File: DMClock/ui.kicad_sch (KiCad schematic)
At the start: 142 parts, among them U3 HV5622PG-G, U4 HV5622PG-G, U5 HV5622PG-G

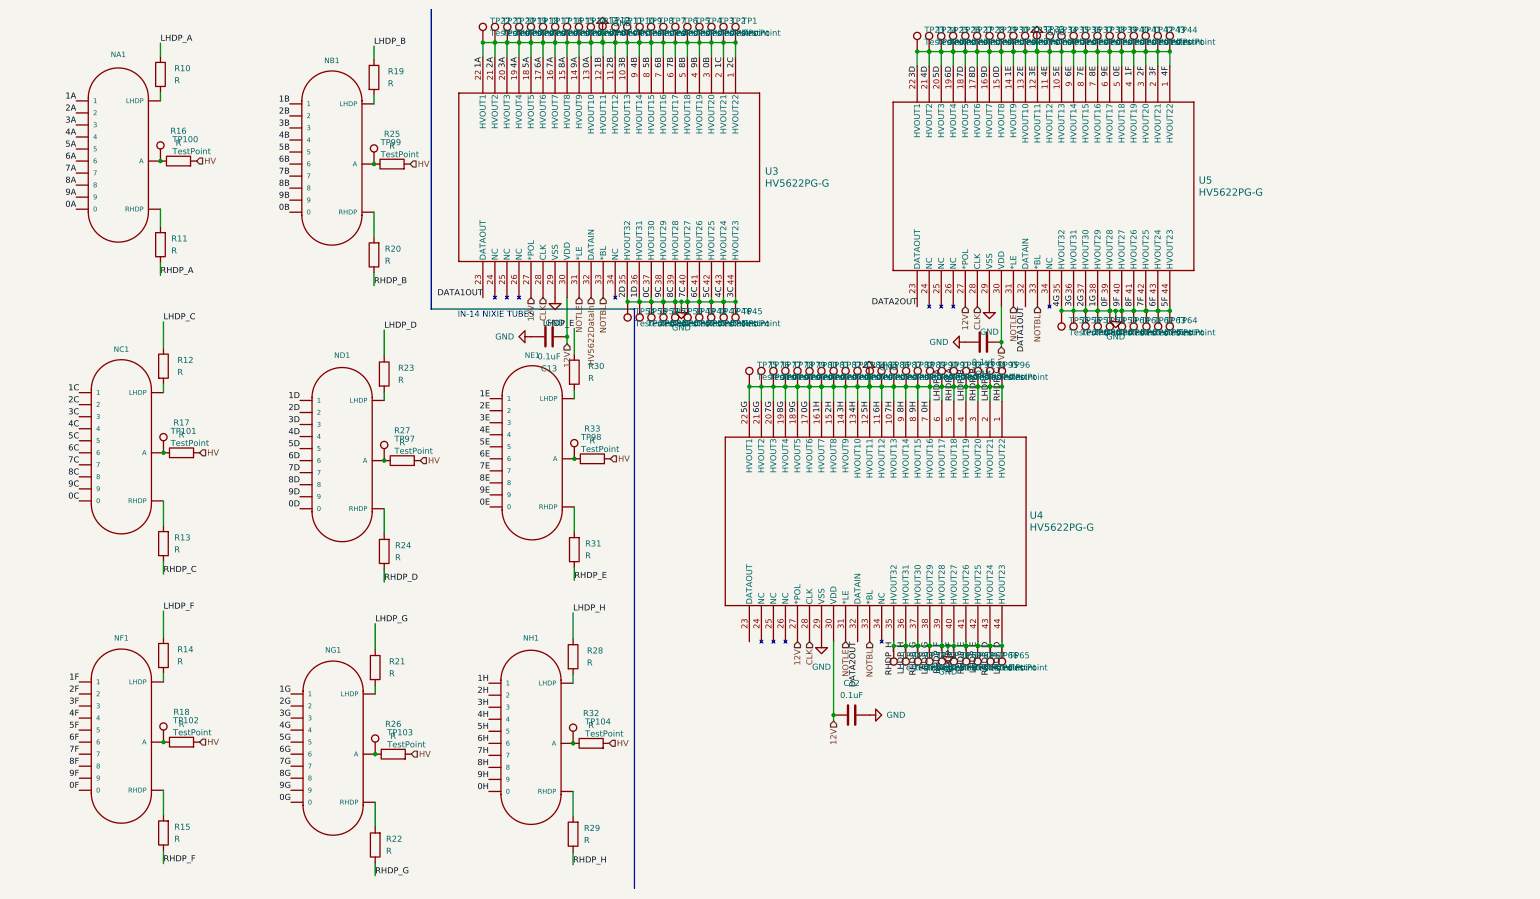
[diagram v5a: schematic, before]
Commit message: added test points, need to fix commas
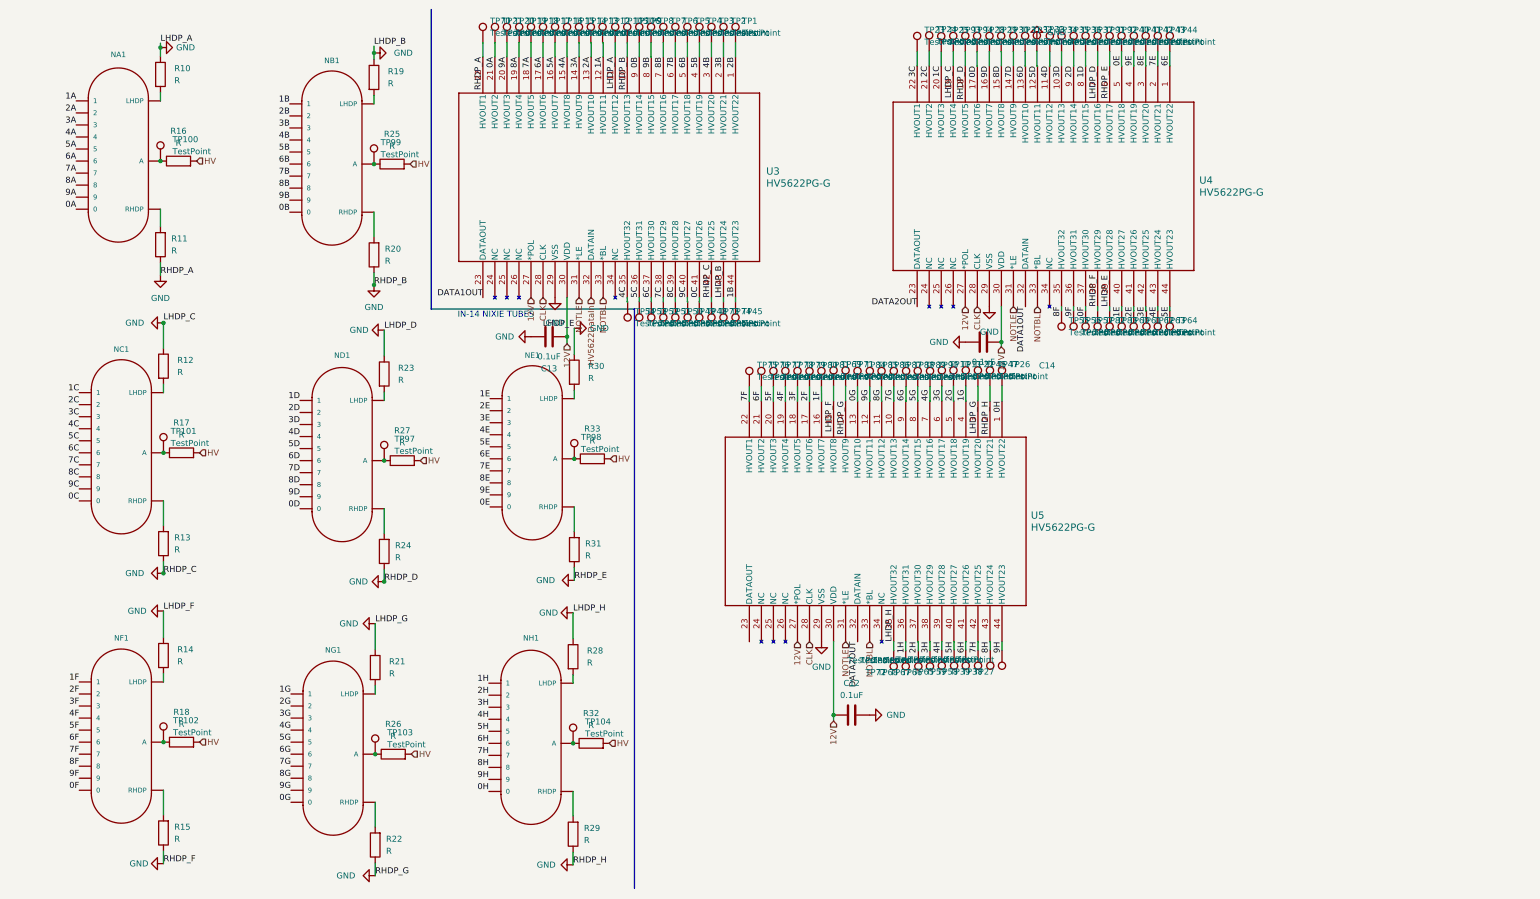
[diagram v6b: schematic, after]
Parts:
- removed TP95, TP96: TestPoint, TestPoint:TestPoint_Pad_D1.5mm, symbol Connector:TestPoint
- added TP105, TP106: TestPoint, TestPoint:TestPoint_Pad_D1.5mm, symbol Connector:TestPoint
- renumbered U5 to U4, U4 to U5
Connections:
- net GND: now also TP105.1, TP106.1; no longer NA1.0, NA1.1, NA1.2, NA1.3, NA1.4, NA1.5, NA1.6, NA1.7, NA1.8, NA1.9, NB1.0, NB1.1, NB1.2, NB1.3, NB1.4, NB1.5, NB1.6, NB1.7, NB1.8, NB1.9, NC1.0, NC1.1, NC1.2, NC1.3, NC1.4, NC1.5, NC1.6, NC1.7, NC1.8, NC1.9, ND1.0, ND1.1, ND1.2, ND1.3, ND1.4, ND1.5, ND1.6, ND1.7, ND1.8, ND1.9, NE1.0, NE1.1, NE1.2, NE1.3, NE1.4, NE1.5, NE1.6, NE1.7, NE1.8, NE1.9, NF1.0, NF1.1, NF1.2, NF1.3, NF1.4, NF1.5, NF1.6, NF1.7, NF1.8, NF1.9, NG1.0, NG1.1, NG1.2, NG1.3, NG1.4, NG1.5, NG1.6, NG1.7, NG1.8, NG1.9, NH1.0, NH1.1, NH1.2, NH1.3, NH1.4, NH1.5, NH1.6, NH1.7, NH1.8, NH1.9, TP1.1, TP10.1, TP11.1, TP12.1, TP13.1, TP14.1, TP15.1, TP16.1, TP17.1, TP18.1, TP19.1, TP2.1, TP20.1, TP21.1, TP22.1, TP23.1, TP24.1, TP25.1, TP26.1, TP27.1, TP28.1, TP29.1, TP3.1, TP30.1, TP31.1, TP32.1, TP33.1, TP34.1, TP35.1, TP36.1, TP37.1, TP38.1, TP39.1, TP4.1, TP40.1, TP41.1, TP42.1, TP43.1, TP44.1, TP45.1, TP48.1, TP49.1, TP5.1, TP50.1, TP51.1, TP52.1, TP53.1, TP54.1, TP55.1, TP56.1, TP57.1, TP58.1, TP59.1, TP6.1, TP60.1, TP61.1, TP62.1, TP63.1, TP64.1, TP65.1, TP66.1, TP67.1, TP68.1, TP7.1, TP75.1, TP76.1, TP77.1, TP78.1, TP79.1, TP8.1, TP80.1, TP81.1, TP84.1, TP85.1, TP86.1, TP87.1, TP88.1, TP89.1, TP9.1, TP90.1, U3.1 (HVOUT22), U3.12 (HVOUT11), U3.13 (HVOUT10), U3.14 (HVOUT9), U3.15 (HVOUT8), U3.16 (HVOUT7), U3.17 (HVOUT6), U3.18 (HVOUT5), U3.19 (HVOUT4), U3.2 (HVOUT21), U3.20 (HVOUT3), U3.21 (HVOUT2), U3.3 (HVOUT20), U3.35 (HVOUT32), U3.36 (HVOUT31), U3.37 (HVOUT30), U3.38 (HVOUT29), U3.39 (HVOUT28), U3.4 (HVOUT19), U3.40 (HVOUT27), U3.41 (HVOUT26), U3.44 (HVOUT23), U3.5 (HVOUT18), U3.6 (HVOUT17), U3.7 (HVOUT16), U3.8 (HVOUT15), U3.9 (HVOUT14), U4.1 (HVOUT22), U4.10 (HVOUT13), U4.11 (HVOUT12), U4.12 (HVOUT11), U4.13 (HVOUT10), U4.14 (HVOUT9), U4.15 (HVOUT8), U4.16 (HVOUT7), U4.17 (HVOUT6), U4.2 (HVOUT21), U4.20 (HVOUT3), U4.21 (HVOUT2), U4.22 (HVOUT1), U4.3 (HVOUT20), U4.35 (HVOUT32), U4.36 (HVOUT31), U4.37 (HVOUT30), U4.4 (HVOUT19), U4.40 (HVOUT27), U4.41 (HVOUT26), U4.42 (HVOUT25), U4.43 (HVOUT24), U4.44 (HVOUT23), U4.5 (HVOUT18), U4.8 (HVOUT15), U4.9 (HVOUT14), U5.1 (HVOUT22), U5.10 (HVOUT13), U5.11 (HVOUT12), U5.12 (HVOUT11), U5.13 (HVOUT10), U5.16 (HVOUT7), U5.17 (HVOUT6), U5.18 (HVOUT5), U5.19 (HVOUT4), U5.20 (HVOUT3), U5.21 (HVOUT2), U5.22 (HVOUT1), U5.36 (HVOUT31), U5.37 (HVOUT30), U5.38 (HVOUT29), U5.39 (HVOUT28), U5.4 (HVOUT19), U5.40 (HVOUT27), U5.41 (HVOUT26), U5.42 (HVOUT25), U5.43 (HVOUT24), U5.44 (HVOUT23), U5.5 (HVOUT18), U5.6 (HVOUT17), U5.7 (HVOUT16), U5.8 (HVOUT15), U5.9 (HVOUT14)
- new net 0A: NA1.0, TP21.1, U3.21 (HVOUT2)
- new net 0B: NB1.0, TP9.1, U3.9 (HVOUT14)
- new net 0C: NC1.0, TP48.1, U3.41 (HVOUT26)
- new net 0D: ND1.0, TP28.1, U4.17 (HVOUT6)
- new net 0E: NE1.0, TP40.1, U4.5 (HVOUT18)
- new net 0F: NF1.0, TP57.1, U4.37 (HVOUT30)
- new net 0G: NG1.0, TP84.1, U5.13 (HVOUT10)
- new net 0H: NH1.0, TP26.1, U5.1 (HVOUT22)
- new net 1A: NA1.1, TP12.1, U3.12 (HVOUT11)
- new net 1B: NB1.1, TP45.1, U3.44 (HVOUT23)
- new net 1C: NC1.1, TP25.1, U4.20 (HVOUT3)
- new net 1D: ND1.1, TP37.1, U4.8 (HVOUT15)
- new net 1E: NE1.1, TP60.1, U4.40 (HVOUT27)
- new net 1F: NF1.1, TP81.1, U5.16 (HVOUT7)
- new net 1G: NG1.1, TP22.1, U5.4 (HVOUT19)
- new net 1H: NH1.1, TP68.1, U5.36 (HVOUT31)
- new net 2A: NA1.2, TP13.1, U3.13 (HVOUT10)
- new net 2B: NB1.2, TP1.1, U3.1 (HVOUT22)
- new net 2C: NC1.2, TP24.1, U4.21 (HVOUT2)
- new net 2D: ND1.2, TP36.1, U4.9 (HVOUT14)
- new net 2E: NE1.2, TP61.1, U4.41 (HVOUT26)
- new net 2F: NF1.2, TP80.1, U5.17 (HVOUT6)
- new net 2G: NG1.2, TP11.1, U5.5 (HVOUT18)
- new net 2H: NH1.2, TP67.1, U5.37 (HVOUT30)
- new net 3A: NA1.3, TP14.1, U3.14 (HVOUT9)
- new net 3B: NB1.3, TP2.1, U3.2 (HVOUT21)
- new net 3C: NC1.3, TP23.1, U4.22 (HVOUT1)
- new net 3D: ND1.3, TP35.1, U4.10 (HVOUT13)
- new net 3E: NE1.3, TP62.1, U4.42 (HVOUT25)
- new net 3F: NF1.3, TP79.1, U5.18 (HVOUT5)
- new net 3G: NG1.3, TP10.1, U5.6 (HVOUT17)
- new net 3H: NH1.3, TP66.1, U5.38 (HVOUT29)
- new net 4A: NA1.4, TP15.1, U3.15 (HVOUT8)
- new net 4B: NB1.4, TP3.1, U3.3 (HVOUT20)
- new net 4C: NC1.4, TP54.1, U3.35 (HVOUT32)
- new net 4D: ND1.4, TP34.1, U4.11 (HVOUT12)
- new net 4E: NE1.4, TP63.1, U4.43 (HVOUT24)
- new net 4F: NF1.4, TP78.1, U5.19 (HVOUT4)
- new net 4G: NG1.4, TP90.1, U5.7 (HVOUT16)
- new net 4H: NH1.4, TP65.1, U5.39 (HVOUT28)
- new net 5A: NA1.5, TP16.1, U3.16 (HVOUT7)
- new net 5B: NB1.5, TP4.1, U3.4 (HVOUT19)
- new net 5C: NC1.5, TP53.1, U3.36 (HVOUT31)
- new net 5D: ND1.5, TP33.1, U4.12 (HVOUT11)
- new net 5E: NE1.5, TP64.1, U4.44 (HVOUT23)
- new net 5F: NF1.5, TP77.1, U5.20 (HVOUT3)
- new net 5G: NG1.5, TP89.1, U5.8 (HVOUT15)
- new net 5H: NH1.5, TP59.1, U5.40 (HVOUT27)
- new net 6A: NA1.6, TP17.1, U3.17 (HVOUT6)
- new net 6B: NB1.6, TP5.1, U3.5 (HVOUT18)
- new net 6C: NC1.6, TP52.1, U3.37 (HVOUT30)
- new net 6D: ND1.6, TP32.1, U4.13 (HVOUT10)
- new net 6E: NE1.6, TP44.1, U4.1 (HVOUT22)
- new net 6F: NF1.6, TP76.1, U5.21 (HVOUT2)
- new net 6G: NG1.6, TP88.1, U5.9 (HVOUT14)
- new net 6H: NH1.6, TP58.1, U5.41 (HVOUT26)
- new net 7A: NA1.7, TP18.1, U3.18 (HVOUT5)
- new net 7B: NB1.7, TP6.1, U3.6 (HVOUT17)
- new net 7C: NC1.7, TP51.1, U3.38 (HVOUT29)
- new net 7D: ND1.7, TP31.1, U4.14 (HVOUT9)
- new net 7E: NE1.7, TP43.1, U4.2 (HVOUT21)
- new net 7F: NF1.7, TP75.1, U5.22 (HVOUT1)
- new net 7G: NG1.7, TP87.1, U5.10 (HVOUT13)
- new net 7H: NH1.7, TP39.1, U5.42 (HVOUT25)
- new net 8A: NA1.8, TP19.1, U3.19 (HVOUT4)
- new net 8B: NB1.8, TP7.1, U3.7 (HVOUT16)
- new net 8C: NC1.8, TP50.1, U3.39 (HVOUT28)
- new net 8D: ND1.8, TP30.1, U4.15 (HVOUT8)
- new net 8E: NE1.8, TP42.1, U4.3 (HVOUT20)
- new net 8F: NF1.8, TP55.1, U4.35 (HVOUT32)
- new net 8G: NG1.8, TP86.1, U5.11 (HVOUT12)
- new net 8H: NH1.8, TP38.1, U5.43 (HVOUT24)
- new net 9A: NA1.9, TP20.1, U3.20 (HVOUT3)
- new net 9B: NB1.9, TP8.1, U3.8 (HVOUT15)
- new net 9C: NC1.9, TP49.1, U3.40 (HVOUT27)
- new net 9D: ND1.9, TP29.1, U4.16 (HVOUT7)
- new net 9E: NE1.9, TP41.1, U4.4 (HVOUT19)
- new net 9F: NF1.9, TP56.1, U4.36 (HVOUT31)
- new net 9G: NG1.9, TP85.1, U5.12 (HVOUT11)
- new net 9H: NH1.9, TP27.1, U5.44 (HVOUT23)

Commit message: started adding traces to hvps logic converter
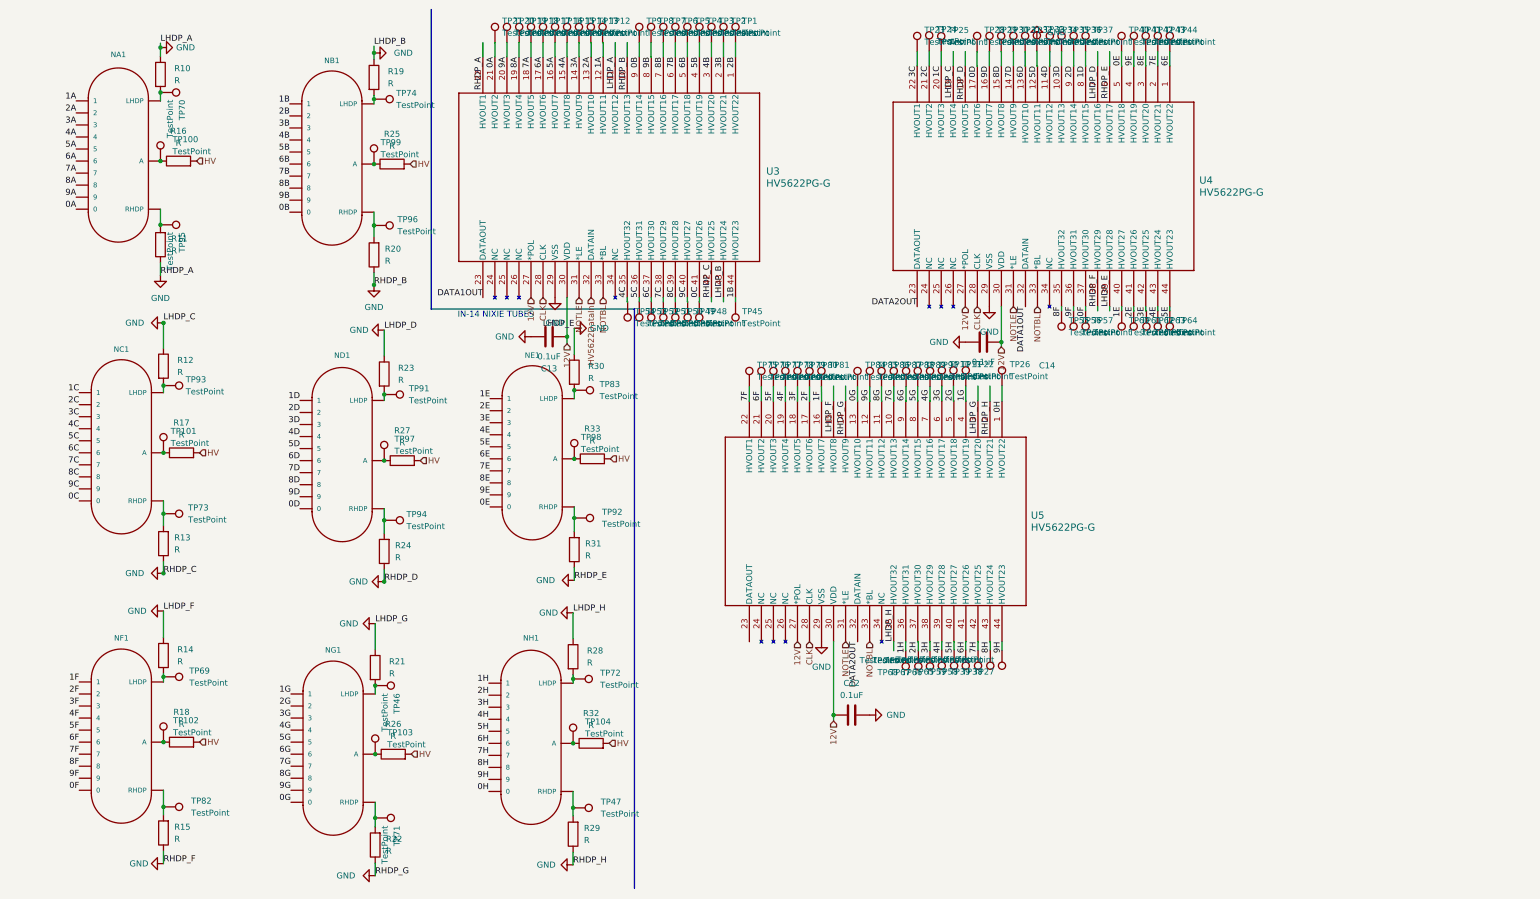
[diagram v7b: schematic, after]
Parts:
- removed TP105, TP106: TestPoint, TestPoint:TestPoint_Pad_D1.5mm, symbol Connector:TestPoint
- added TP95, TP96: TestPoint, TestPoint:TestPoint_Pad_D1.5mm, symbol Connector:TestPoint
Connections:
- net GND: no longer TP46.1, TP47.1, TP69.1, TP70.1, TP71.1, TP72.1, TP73.1, TP74.1, TP82.1, TP83.1, TP91.1, TP92.1, TP93.1, TP94.1
- net at NA1.RHDP, R11.2: now also TP95.1
- net at NE1.LHDP, R30.2: now also TP83.1
- net at NG1.RHDP, R22.2: now also TP71.1
- net at ND1.RHDP, R24.2: now also TP94.1
- net at NB1.RHDP, R20.2: now also TP96.1
- net at NH1.LHDP, R28.2: now also TP72.1
- net at NE1.RHDP, R31.2: now also TP92.1
- net at NH1.RHDP, R29.2: now also TP47.1
- net at NC1.LHDP, R12.2: now also TP93.1
- net at NC1.RHDP, R13.2: now also TP73.1
- net at ND1.LHDP, R23.2: now also TP91.1
- net at NF1.LHDP, R14.2: now also TP69.1
- net at NF1.RHDP, R15.2: now also TP82.1
- net at NA1.LHDP, R10.2: now also TP70.1
- net at NB1.LHDP, R19.2: now also TP74.1
- net at NG1.LHDP, R21.2: now also TP46.1

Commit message: first layer done, needs optimizations
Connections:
- net GND: no longer R10.1, R11.1, R12.1, R13.1, R14.1, R15.1, R19.1, R20.1, R21.1, R22.1, R23.1, R24.1, R28.1, R29.1, R30.1, R31.1, U3.10 (HVOUT13), U3.11 (HVOUT12), U3.22 (HVOUT1), U3.42 (HVOUT25), U3.43 (HVOUT24), U4.18 (HVOUT5), U4.19 (HVOUT4), U4.38 (HVOUT29), U4.39 (HVOUT28), U4.6 (HVOUT17), U4.7 (HVOUT16), U5.14 (HVOUT9), U5.15 (HVOUT8), U5.2 (HVOUT21), U5.3 (HVOUT20), U5.35 (HVOUT32)
- new net LHDP_A: R10.1, U3.11 (HVOUT12)
- new net LHDP_B: R19.1, U3.43 (HVOUT24)
- new net LHDP_C: R12.1, U4.19 (HVOUT4)
- new net LHDP_D: R23.1, U4.7 (HVOUT16)
- new net LHDP_E: R30.1, U4.39 (HVOUT28)
- new net LHDP_F: R14.1, U5.15 (HVOUT8)
- new net LHDP_G: R21.1, U5.3 (HVOUT20)
- new net LHDP_H: R28.1, U5.35 (HVOUT32)
- new net RHDP_A: R11.1, U3.22 (HVOUT1)
- new net RHDP_B: R20.1, U3.10 (HVOUT13)
- new net RHDP_C: R13.1, U3.42 (HVOUT25)
- new net RHDP_D: R24.1, U4.18 (HVOUT5)
- new net RHDP_E: R31.1, U4.6 (HVOUT17)
- new net RHDP_F: R15.1, U4.38 (HVOUT29)
- new net RHDP_G: R22.1, U5.14 (HVOUT9)
- new net RHDP_H: R29.1, U5.2 (HVOUT21)
